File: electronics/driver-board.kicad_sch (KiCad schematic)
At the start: 58 parts, among them J1 Conn_01x01_Socket, J10 USB_C_Receptacle_USB2.0, J3 Conn_01x06, J4 Qwiic_RA, J5 Conn_02x03_Counter_Clockwise, J9 Conn_01x01_Socket, SW1 SW_Push, SW2 SW_Push, SW3 SW_Push, SW4 SW_Push, U1 LMR16006YQ3, U3 ESP32-C6-MINI-1/U, U5 TMC5240-TSSOP38, U7 AS5047D

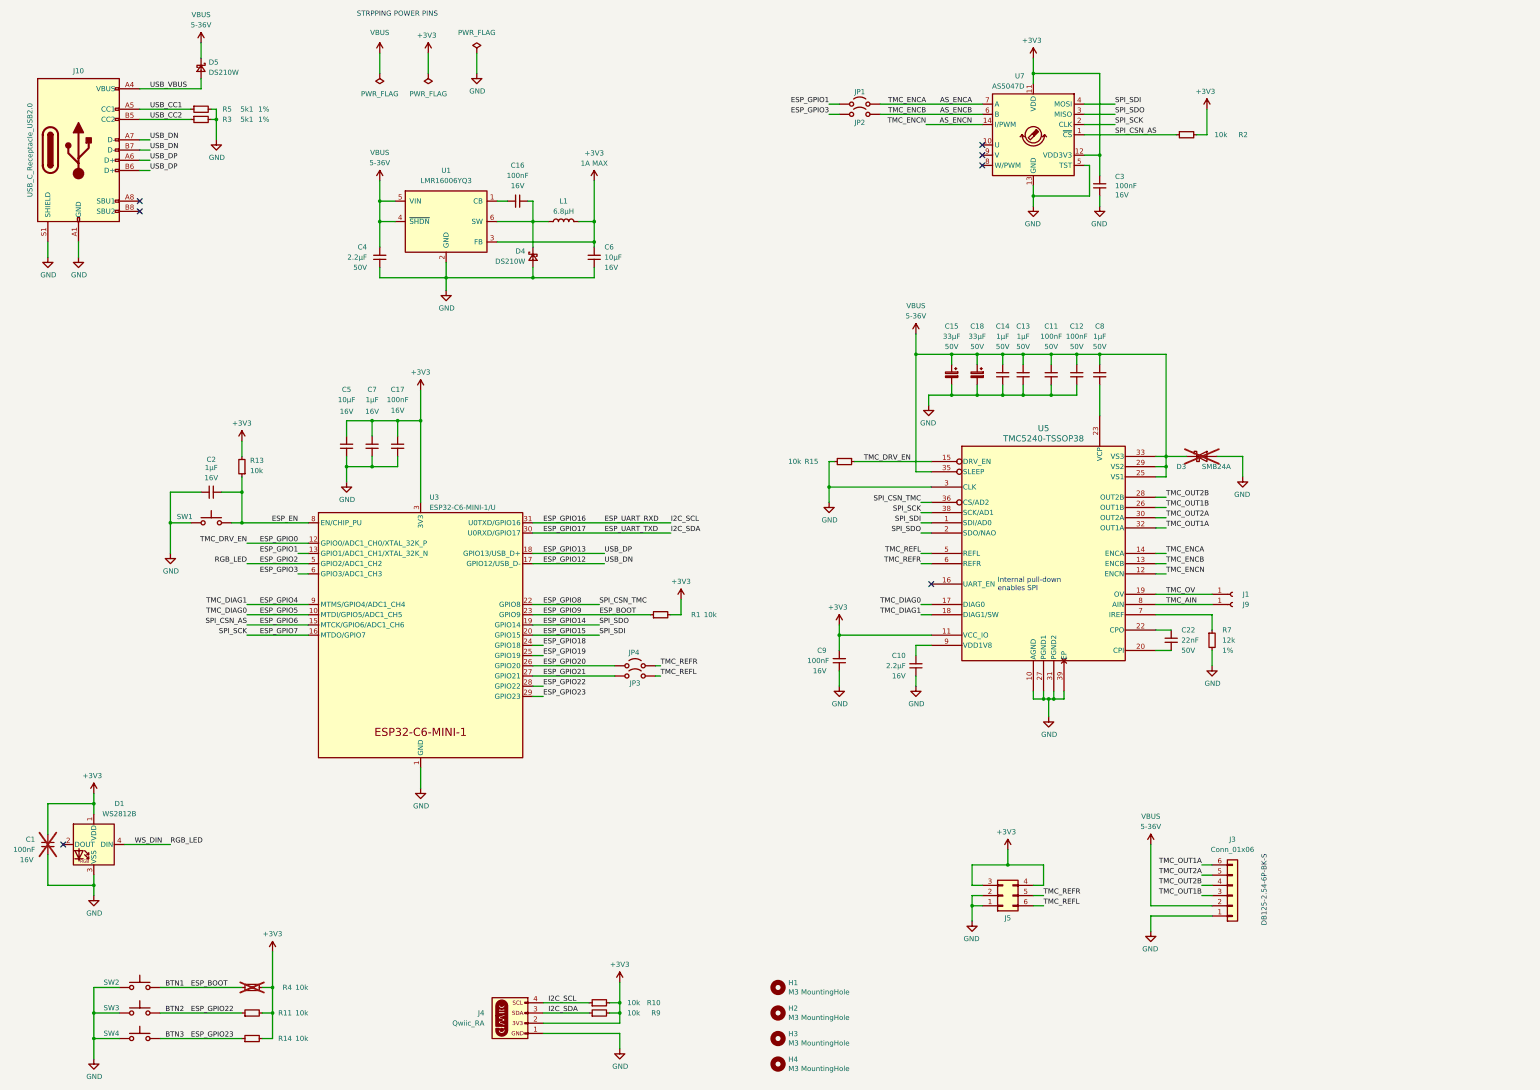
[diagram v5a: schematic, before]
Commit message: added ldo for USB
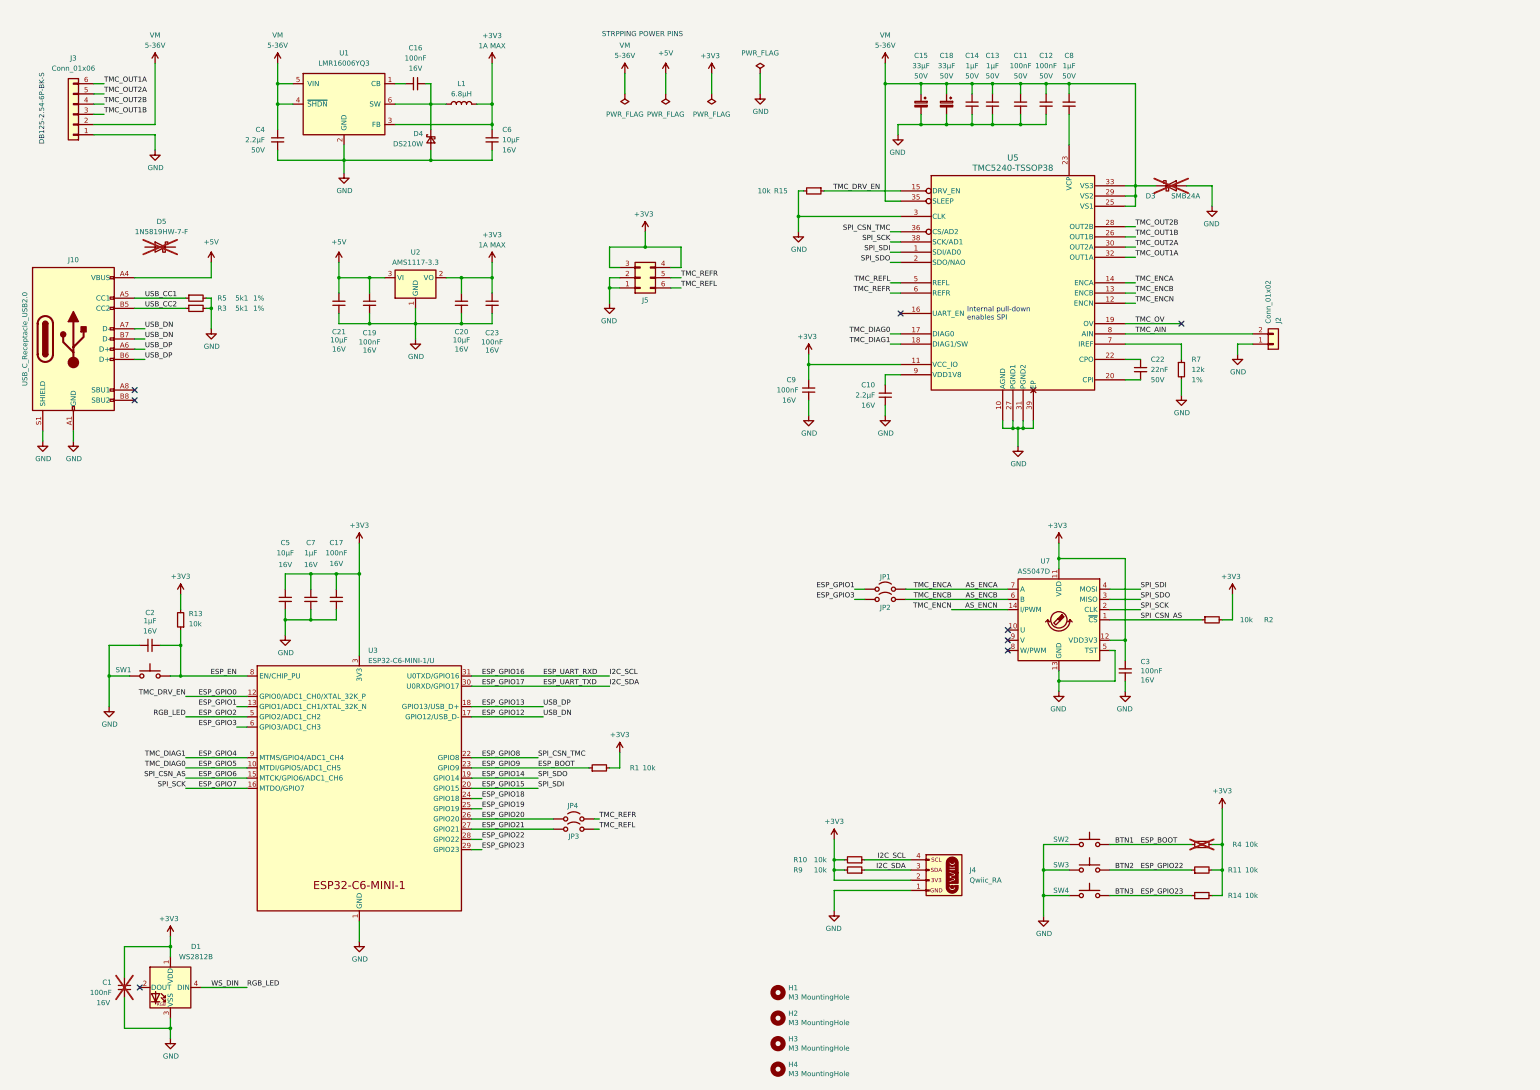
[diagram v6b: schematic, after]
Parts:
- removed D5: DS210W, Diode_SMD:D_SOD-123F, symbol Device:D_Schottky_Small
- removed J1, J9: Conn_01x01_Socket, TestPoint:TestPoint_Pad_D2.0mm, symbol Connector:Conn_01x01_Socket
- added C19, C23: 100nF, Capacitor_SMD:C_0603_1608Metric, symbol Device:C_Small
- added C20, C21: 10µF, Capacitor_SMD:C_0603_1608Metric, symbol Device:C_Small
- added D5: 1N5819HW-7-F, Diode_SMD:D_SOD-123, symbol Diode:1N5819
- added J2: Conn_01x02, Connector_PinHeader_2.54mm:PinHeader_1x02_P2.54mm_Vertical, symbol Connector_Generic:Conn_01x02
- added U2: AMS1117-3.3, Package_TO_SOT_SMD:SOT-223-3_TabPin2, symbol Regulator_Linear:AMS1117-3.3
- D1: footprint LED_SMD:LED_SK6812_EC15_1.5x1.5mm -> LED_SMD:LED_WS2812B-2020_PLCC4_2.0x2.0mm
- R1, R15, R3, R5: footprint Resistor_SMD:R_0603_1608Metric -> Capacitor_SMD:C_0402_1005Metric; Package 0603 -> 0402
- R10, R11, R13, R14, R2, R4, R9: footprint Resistor_SMD:R_0603_1608Metric -> Capacitor_SMD:C_0402_1005Metric
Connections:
- net +3V3: now also C20.2, C23.1, U2.2 (VO)
- net GND: now also C19.2, C20.1, C21.1, C23.2, J2.1 (Pin_1), U2.1 (GND)
- net TMC_AIN: now also J2.2 (Pin_2)
- net USB_VBUS renamed +5V
- net +5V: now also C19.1, C21.2, U2.3 (VI)
- net VBUS renamed VM
- no-connect marks 7 -> 8
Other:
- moved on the sheet: C1, C10, C11, C12, C13, C14, C15, C16, C17, C18, C2, C22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

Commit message: reworked layout a bit
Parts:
- removed D5: 1N5819HW-7-F, Diode_SMD:D_SOD-123, symbol Diode:1N5819
- removed J2: Conn_01x02, Connector_PinHeader_2.54mm:PinHeader_1x02_P2.54mm_Vertical, symbol Connector_Generic:Conn_01x02
- added C24: 100nF, Capacitor_SMD:C_0603_1608Metric, symbol Device:C_Small
- added D2, D6: LESD5D5, Diode_SMD:D_SOD-523, symbol Device:D_TVS
- added R6: 10k, Resistor_SMD:R_0402_1005Metric, symbol Device:R_Small
- added TH1: MF55 103F3950, symbol Device:Thermistor_NTC
- C1: footprint Capacitor_SMD:C_0603_1608Metric -> Capacitor_SMD:C_0402_1005Metric; now fitted; now in the parts list
- R1, R10, R11, R13, R14, R15, R2, R3, R4, R5, R9: footprint Capacitor_SMD:C_0402_1005Metric -> Resistor_SMD:R_0402_1005Metric
- R7: footprint Resistor_SMD:R_0603_1608Metric -> Resistor_SMD:R_0402_1005Metric
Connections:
- net +3V3: now also R6.2
- net ESP_GPIO12: now also D2.2 (A2)
- net ESP_GPIO13: now also D6.2 (A2)
- net ESP_GPIO14: now also U5.1 (SDI/AD0), U7.4 (MOSI); no longer U5.2 (SDO/NAO), U7.3 (MISO)
- net ESP_GPIO15: now also U5.36 (CS/AD2); no longer U5.1 (SDI/AD0), U7.4 (MOSI)
- net ESP_GPIO6: now also U5.2 (SDO/NAO), U7.3 (MISO); no longer R2.1, U7.1 (~{CS})
- net ESP_GPIO7: now also R2.1, U7.1 (~{CS}); no longer U5.38 (SCK/AD1), U7.2 (CLK)
- net ESP_GPIO8: now also U5.38 (SCK/AD1), U7.2 (CLK); no longer U5.36 (CS/AD2)
- net GND: now also C24.1, D2.1 (A1), D6.1 (A1), TH1.2
- net TMC_AIN: now also C24.2, R6.1, TH1.1
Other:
- moved on the sheet: C10, C11, C12, C13, C14, C15, C16, C17, C18, C19, C2, C20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

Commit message: wip usb jtag and power connectors
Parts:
- removed J3: Conn_01x06, TerminalBlock_Phoenix:TerminalBlock_Phoenix_MPT-0,5-6-2.54_1x06_P2.54mm_Horizontal, symbol SparkFun-Connector:Conn_01x06
- removed J5: Conn_02x03_Counter_Clockwise, Connector_PinHeader_2.54mm:PinHeader_2x03_P2.54mm_Vertical, symbol Connector_Generic:Conn_02x03_Counter_Clockwise
- added J1: Conn_01x02, Connector_PinHeader_2.00mm:PinHeader_1x02_P2.00mm_Vertical_SMD_Pin1Left, symbol SparkFun-Connector:Conn_01x02
- added J2, J7: Conn_01x03, Connector_JST:JST_SH_SM03B-SRSS-TB_1x03-1MP_P1.00mm_Horizontal, symbol Connector_Generic:Conn_01x03
- added J5: Conn_01x02, Connector_JST:JST_PH_S2B-PH-K_1x02_P2.00mm_Horizontal, symbol Connector_Generic:Conn_01x02
- added J6: Conn_01x04, Connector_JST:JST_PH_S4B-PH-K_1x04_P2.00mm_Horizontal, symbol Connector_Generic:Conn_01x04
- added R12, R8: 10k, Resistor_SMD:R_0402_1005Metric, symbol Device:R_Small
- J10: footprint Connector_USB:USB_C_Receptacle_GCT_USB4105-xx-A_16P_TopMnt_Horizontal -> Connector_USB:USB_C_Receptacle_JAE_DX07S024WJ3R400; LCSC (none) -> C22383823; Manf (none) -> G-Switch; Manf# (none) -> GT-USB-7036A
- J4: footprint SparkFun-Connector:JST04_1MM_Vertical -> SparkFun-Connector:JST_SMD_1.0mm-4_RA; LCSC C160404 -> (none); Manf JST -> (none); Manf# SM04B-SRSS-TB -> (none)
- R11, R14: now not fitted; now left out of the parts list
- SW2: footprint Slimc_Button_Switch_SMD:SW_Push_1P1T_TS-1145-X-B -> Button_Switch_SMD:SW_SPST_B3U-1000P
- SW3, SW4: footprint Slimc_Button_Switch_SMD:SW_Push_1P1T_TS-1145-X-B -> Button_Switch_SMD:SW_SPST_B3U-1000P; now not fitted; now left out of the parts list
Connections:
- net +3V3: now also J2.2 (Pin_2), J7.2 (Pin_2), R12.2, R8.2
- net GND: now also J1.1 (Pin_1), J2.1 (Pin_1), J5.1 (Pin_1), J7.1 (Pin_1); no longer TH1.2
- net TMC_AIN: now also J1.2 (Pin_2); no longer TH1.1
- net TMC_OUT1A: now also J6.4 (Pin_4)
- net TMC_OUT1B: now also J6.2 (Pin_2)
- net TMC_OUT2A: now also J6.3 (Pin_3)
- net TMC_OUT2B: now also J6.1 (Pin_1)
- net TMC_REFL: now also J2.3 (Pin_3), R8.1
- net TMC_REFR: now also J7.3 (Pin_3), R12.1
- net VM: now also J5.2 (Pin_2)
- net at J4.NC1 (NC): no longer J4.NC2 (NC)
- net BTN1 renamed ESP_BOOT
- net BTN2 renamed ESP_GPIO22
- net BTN3 renamed ESP_GPIO23
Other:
- moved on the sheet: C10, C11, C12, C13, C14, C15, C18, C22, C24, C8, C9, D3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
